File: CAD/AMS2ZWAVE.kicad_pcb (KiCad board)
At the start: 2 copper layers, 33 x 98.1 mm, 52 parts, among them J1 RJ45_Shielded, J2 Conn_Coaxial, J3 mini simplicity, J4 Conn_01x05_Male, SW1 SW_Push, U1 NCN5150DR2G, U2 LM358, U3 MAX17531AUB+T, U4 ZGM130S

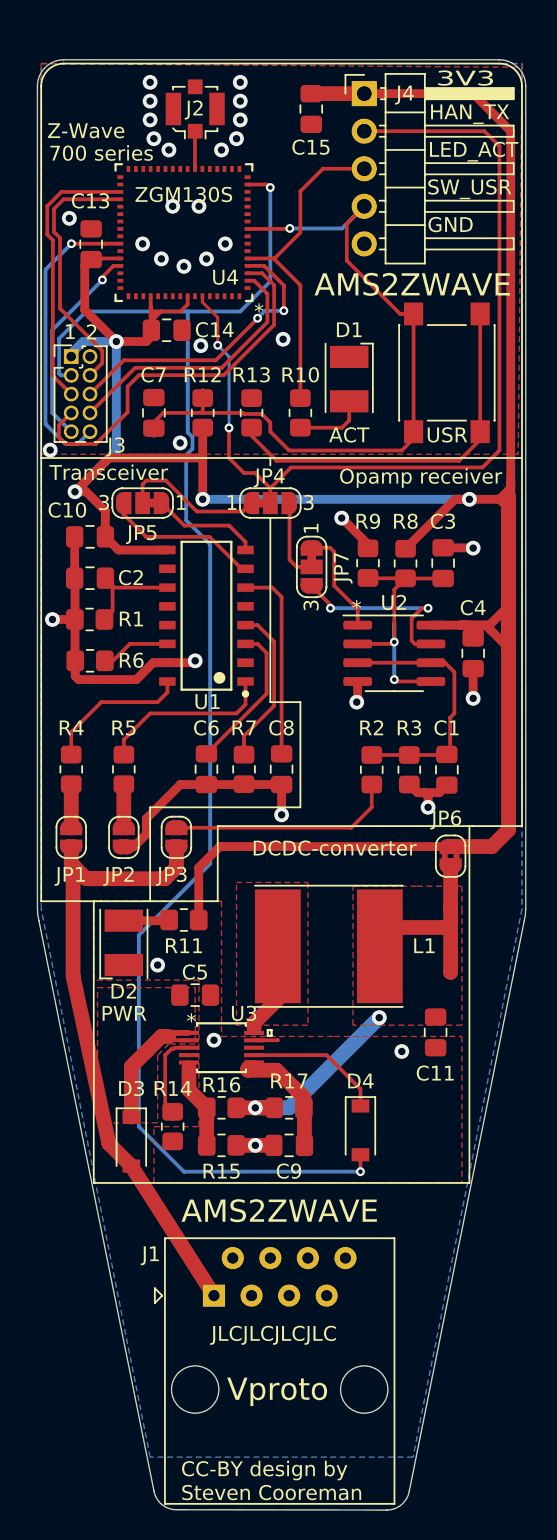
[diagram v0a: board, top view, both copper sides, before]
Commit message: PCB iteration 2
* Added inrush current limiter
* Added footprint to use BRD4202 instead of soldering down ZGM130S
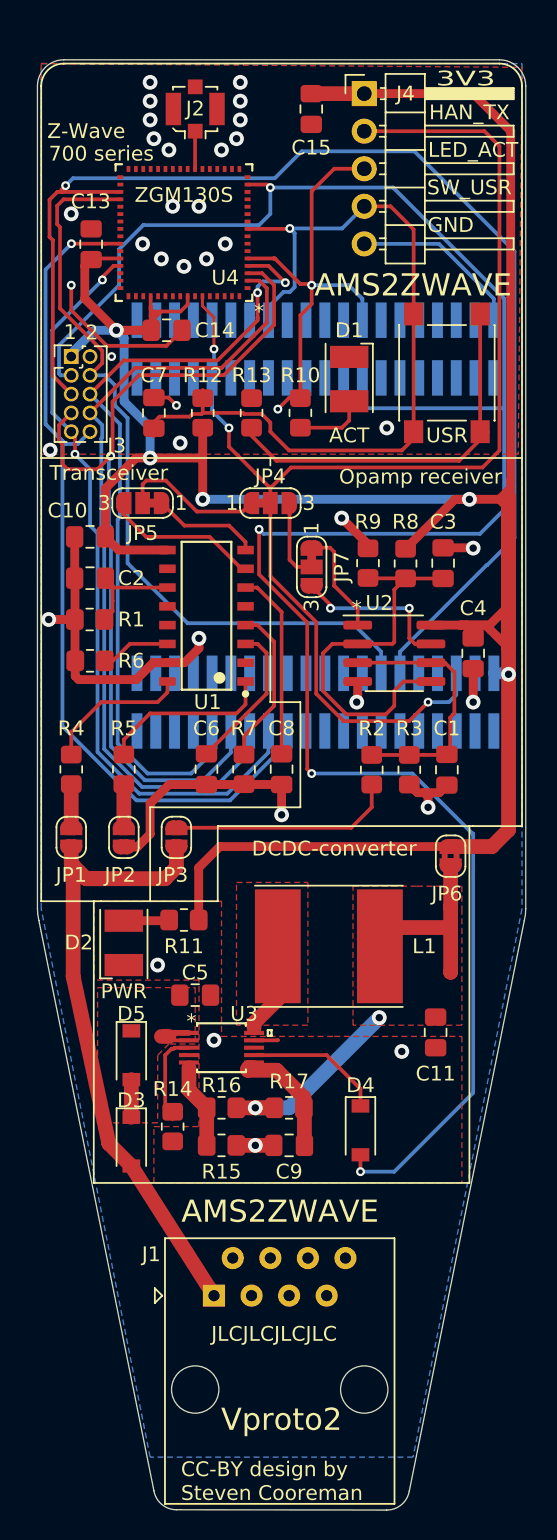
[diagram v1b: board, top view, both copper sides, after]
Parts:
- added D5: NSI50010, Diode_SMD:D_SOD-123, F.Cu at (122.4, 115.3)
- added J5: BRD_upper, Connector_PinHeader_1.27mm:PinHeader_2x20_P1.27mm_Vertical_SMD, B.Cu at (134.9, 67.6)
- added J6: BRD_lower, Connector_PinHeader_1.27mm:PinHeader_2x20_P1.27mm_Vertical_SMD, B.Cu at (134.9, 91.4)
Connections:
- D3 pad 1: Net-(C5-Pad1) -> Net-(D3-Pad1)
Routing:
- net VCOM_TX: track 18.7 -> 85.2 mm, vias 0 -> 1
- net nRST: track 102.8 -> 148.0 mm, vias 2 -> 4
- net PTI_DATA: track 20.1 -> 59.7 mm
- net PTI_FRAME: track 13.9 -> 51.6 mm, vias 1 -> 2
- net SWCLK: track 18.2 -> 54.8 mm
- net VCOM_RX: track 17.7 -> 53.0 mm
- net SWDIO: track 25.9 -> 60.3 mm, vias 0 -> 1
- net SWO: track 20.2 -> 54.5 mm
- net HAN-: track 50.5 -> 77.0 mm, vias 34 -> 36
- net HAN_TX: track 63.0 -> 89.0 mm, vias 2 -> 3
- net Net-(C5-Pad1): track 16.3 -> 5.67 mm
- net LED_ACT: track 21.7 -> 30.7 mm, vias 0 -> 2
- net Vref: track 19.9 -> 26.9 mm, vias 2 -> 0
- net SW_USR: track 49.4 -> 56.2 mm
- net +3V3: track 207.8 -> 202.9 mm, vias 4 -> 5
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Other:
- board text added: "Vproto2"
- board text removed: "Vproto"

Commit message: Update to v2 PCB
* Increased DCDC switching frequency to 600kHz
* Added resistor divider for setting UVLO to 10V
* Added solderjumper for DCDC mode
* Added bulk capacitor to smooth out 12V swings on the input line
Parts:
- added C12: 1n, Capacitor_SMD:C_0805_2012Metric_Pad1.18x1.45mm_HandSolder, F.Cu at (125.3, 120.5)
- added C16: 33u, Capacitor_Tantalum_SMD:CP_EIA-2012-12_Kemet-R_Pad1.30x1.05mm_HandSolder, F.Cu at (125.3, 110.5)
- added JP8: SolderJumper_2_Open, Jumper:SolderJumper-2_P1.3mm_Open_RoundedPad1.0x1.5mm, F.Cu at (139.4, 115.1)
- added R18: 1M, Resistor_SMD:R_0805_2012Metric_Pad1.20x1.40mm_HandSolder, F.Cu at (123.2, 114.1)
- added R19: 130k, Resistor_SMD:R_0805_2012Metric_Pad1.20x1.40mm_HandSolder, F.Cu at (123.3, 120.5)
- C1: value 100n -> 1n
- JP1, JP2: footprint Jumper:SolderJumper-2_P1.3mm_Open_RoundedPad1.0x1.5mm -> Jumper:SolderJumper-2_P1.3mm_Bridged_RoundedPad1.0x1.5mm
- moved R14 2.07 mm to (127.3, 120.5)
- moved C9 1.78 mm to (134.9, 121.4)
- moved R15 1.78 mm to (130.3, 121.4)
- moved R16 1.78 mm to (130.3, 118.9)
- moved R17 1.78 mm to (134.9, 118.9)
- moved C5 1.76 mm to (128.5, 111.2)
- moved D4 1.52 mm to (139.4, 120.4)
- moved U3 1.52 mm to (130.0, 114.8)
- moved D5 1.43 mm to (121.0, 115.0)
- moved D3 1.40 mm to (121.0, 121.0)
- moved L1 1.14 mm to (136.8, 107.4)
- moved C11 0.58 mm to (143.3, 113.3)
- moved D2 0.38 mm to (121.5, 107.7)
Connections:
- C5 pad 1: Net-(C5-Pad1) -> Net-(C16-Pad1)
- D5 pad 1: Net-(C5-Pad1) -> Net-(C16-Pad1)
- U3 pad 1: Net-(C5-Pad1) -> Net-(C16-Pad1)
- U3 pad 2: Net-(C5-Pad1) -> Net-(C12-Pad1)
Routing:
- net Net-(C12-Pad1): track 0.00 -> 11.9 mm
- net +VSW: track 26.2 -> 16.5 mm
- net Net-(JP8-Pad2): track 0.00 -> 6.62 mm
- net Net-(C5-Pad1): track 5.67 -> 0.00 mm
- net nRST: track 148.0 -> 146.4 mm
- net HAN+: track 43.2 -> 44.2 mm
- net Net-(R14-Pad1): track 6.36 -> 5.78 mm
- added copper zone on F.Cu, net Net-(C16-Pad1)
- removed copper zone on F.Cu, net Net-(C5-Pad1)

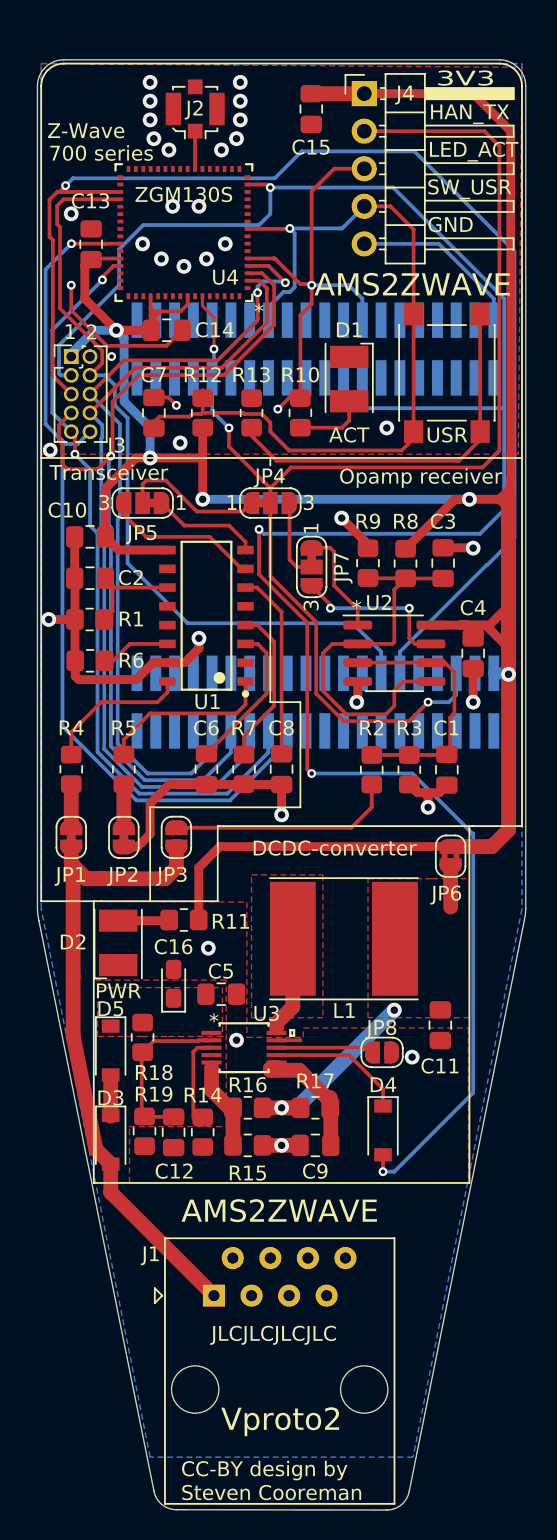
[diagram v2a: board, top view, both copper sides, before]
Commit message: Update to proto v2
* Added edgemount SMA in addition to U.FL for antenna flexibility
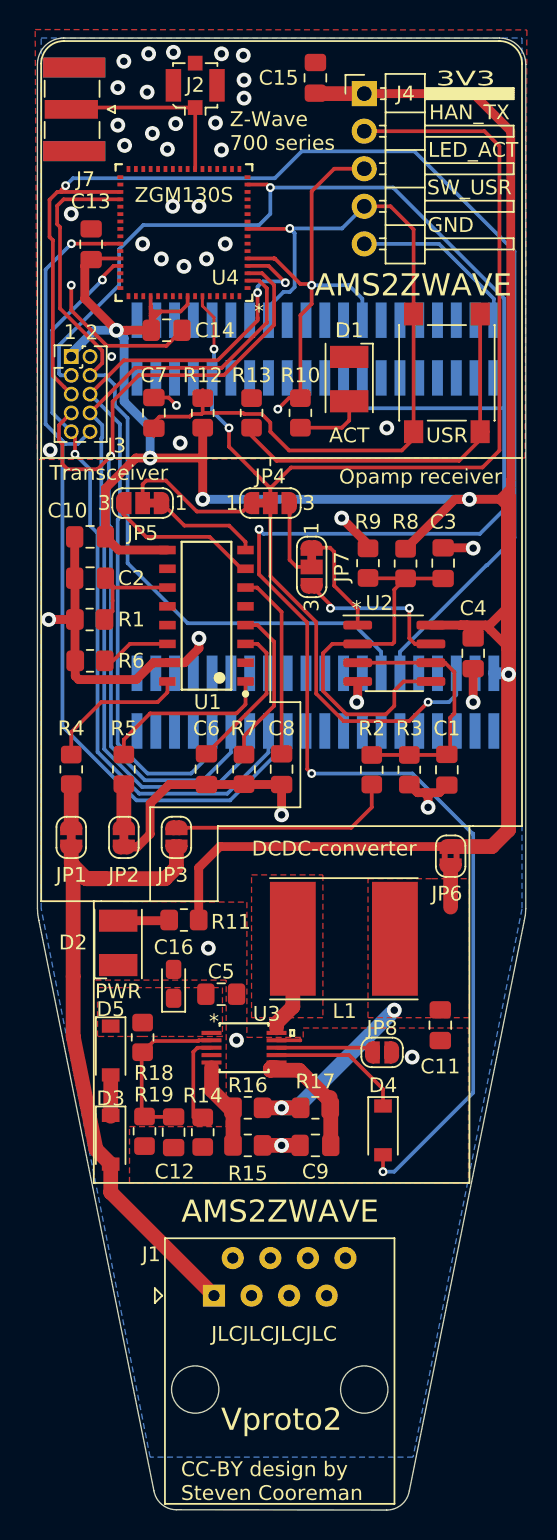
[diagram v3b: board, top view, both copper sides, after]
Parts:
- added J7: Conn_Coaxial, Connector_Coaxial:SMA_Samtec_SMA-J-P-X-ST-EM1_EdgeMount, F.Cu at (118.6, 51.4)
- R14: value 140k -> 69.8k
- moved C15 2.13 mm to (134.9, 49.2), turned to 90 degrees
- moved J2 1.60 mm to (126.7, 49.7)
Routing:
- net Net-(J2-Pad1): track 2.56 -> 12.5 mm
- net HAN-: vias 36 -> 42
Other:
- board size 33 x 98.1 mm -> 33 x 99.5 mm
- board text added: "Z-Wave 700 series"
- board text removed: "700 series"
- board text removed: "Z-Wave"

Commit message: Update to proto v2
* Added test points for LGA pads bordering on in-use pads, to avoid them from coming loose when too much heat is applied
* Moved SMA edge connector around, it makes more sense to have it at the top
* Tidied layout
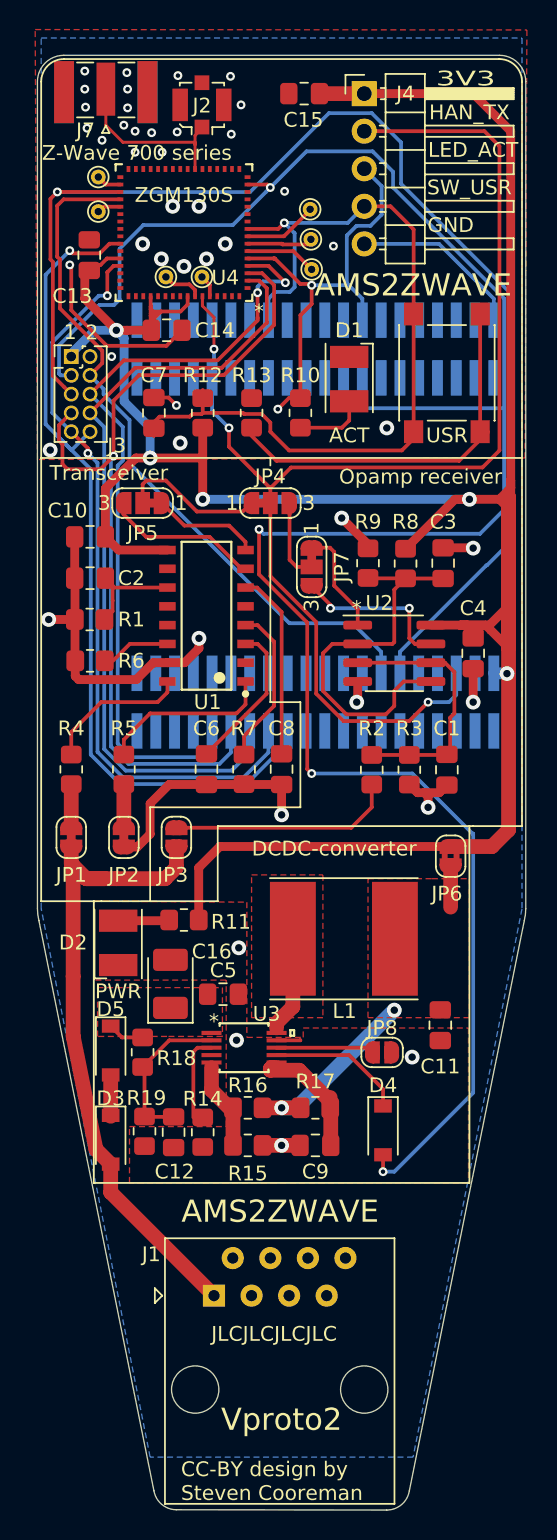
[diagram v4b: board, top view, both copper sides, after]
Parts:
- added TP1: TestPoint, TestPoint:TestPoint_THTPad_D1.0mm_Drill0.5mm, F.Cu at (134.6, 62.2)
- added TP2: TestPoint, TestPoint:TestPoint_THTPad_D1.0mm_Drill0.5mm, F.Cu at (134.6, 60.1)
- added TP3: TestPoint, TestPoint:TestPoint_THTPad_D1.0mm_Drill0.5mm, F.Cu at (134.5, 58.1)
- added TP4: TestPoint, TestPoint:TestPoint_THTPad_D1.0mm_Drill0.5mm, F.Cu at (120.2, 58.3)
- added TP5: TestPoint, TestPoint:TestPoint_THTPad_D1.0mm_Drill0.5mm, F.Cu at (120.2, 55.9)
- added TP6: TestPoint, TestPoint:TestPoint_THTPad_D1.0mm_Drill0.5mm, F.Cu at (127.2, 62.7)
- added TP7: TestPoint, TestPoint:TestPoint_THTPad_D1.0mm_Drill0.5mm, F.Cu at (124.8, 62.7)
- C16: footprint Capacitor_Tantalum_SMD:CP_EIA-2012-12_Kemet-R_Pad1.30x1.05mm_HandSolder -> Capacitor_Tantalum_SMD:CP_EIA-3528-12_Kemet-T_Pad1.50x2.35mm_HandSolder
- moved J7 2.43 mm to (120.7, 50.2), turned to 180 degrees
- moved J2 1.40 mm to (127.2, 51.1)
- moved C15 1.31 mm to (134.1, 50.3), turned to 180 degrees
- moved R18 1.00 mm to (123.2, 115.1)
- moved C13 0.75 mm to (119.6, 61.2)
- moved C16 0.22 mm to (125.1, 110.5)
- moved C5 0.12 mm to (128.6, 111.2)
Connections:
- U4 pad 40: Net-(U4-Pad40) -> HAN-
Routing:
- net Net-(TP3-Pad1): track 0.00 -> 5.02 mm
- net Net-(TP1-Pad1): track 0.00 -> 4.93 mm
- net VCOM_RX: track 53.0 -> 48.3 mm
- net Net-(TP2-Pad1): track 0.00 -> 4.37 mm
- net Net-(TP7-Pad1): track 0.00 -> 2.75 mm
- net Net-(C16-Pad1): track 0.00 -> 2.48 mm
- net nRST: track 146.4 -> 148.6 mm
- net VCOM_TX: track 85.2 -> 87.2 mm
- net Net-(TP5-Pad1): track 0.00 -> 1.70 mm
- net Net-(TP4-Pad1): track 0.00 -> 1.63 mm
- net Net-(TP6-Pad1): track 0.00 -> 1.52 mm
- net HAN-: track 77.0 -> 78.4 mm, vias 42 -> 45
- net +3V3: track 202.9 -> 201.7 mm
- net SWCLK: track 54.8 -> 53.9 mm
- net Net-(C12-Pad1): track 11.9 -> 10.9 mm
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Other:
- board size 33 x 99.5 mm -> 33 x 98.4 mm
